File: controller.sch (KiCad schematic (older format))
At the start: 29 parts, among them Q1 Q_PMOS_SGD, Q2 Q_PMOS_SGD, SW1 L1, SW2 L2, SW3 Select, SW4 Start, SW5 R2, SW6 R1, U1 Thumbstick, U2 dpad-cross-trace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

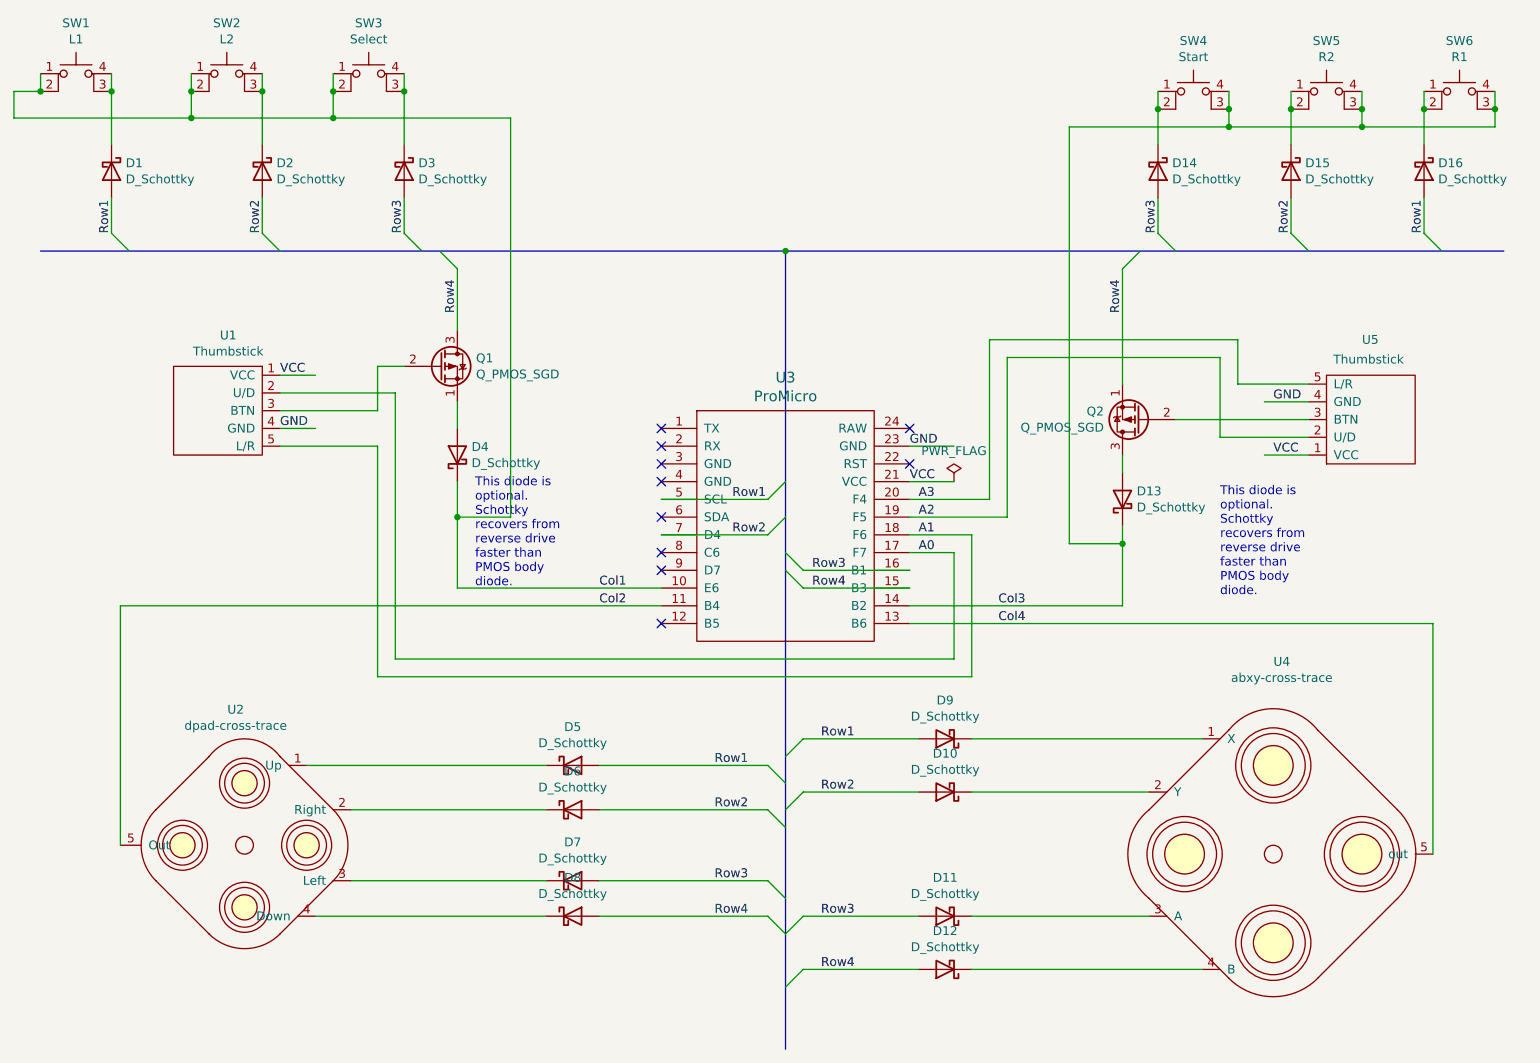
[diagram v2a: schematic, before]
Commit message: Move most PWR_FLAGs into corner and use GNDA.
Use GNDA power pin in the audio subsystem instead of "agnd" sheet label.
Re-examine application of PWR_FLAGS after reading the wiki page.

Change the symbol for thumbstick in controller subsystem to reflect that
it's actually the FPC connector and not actually the thumbstick module.
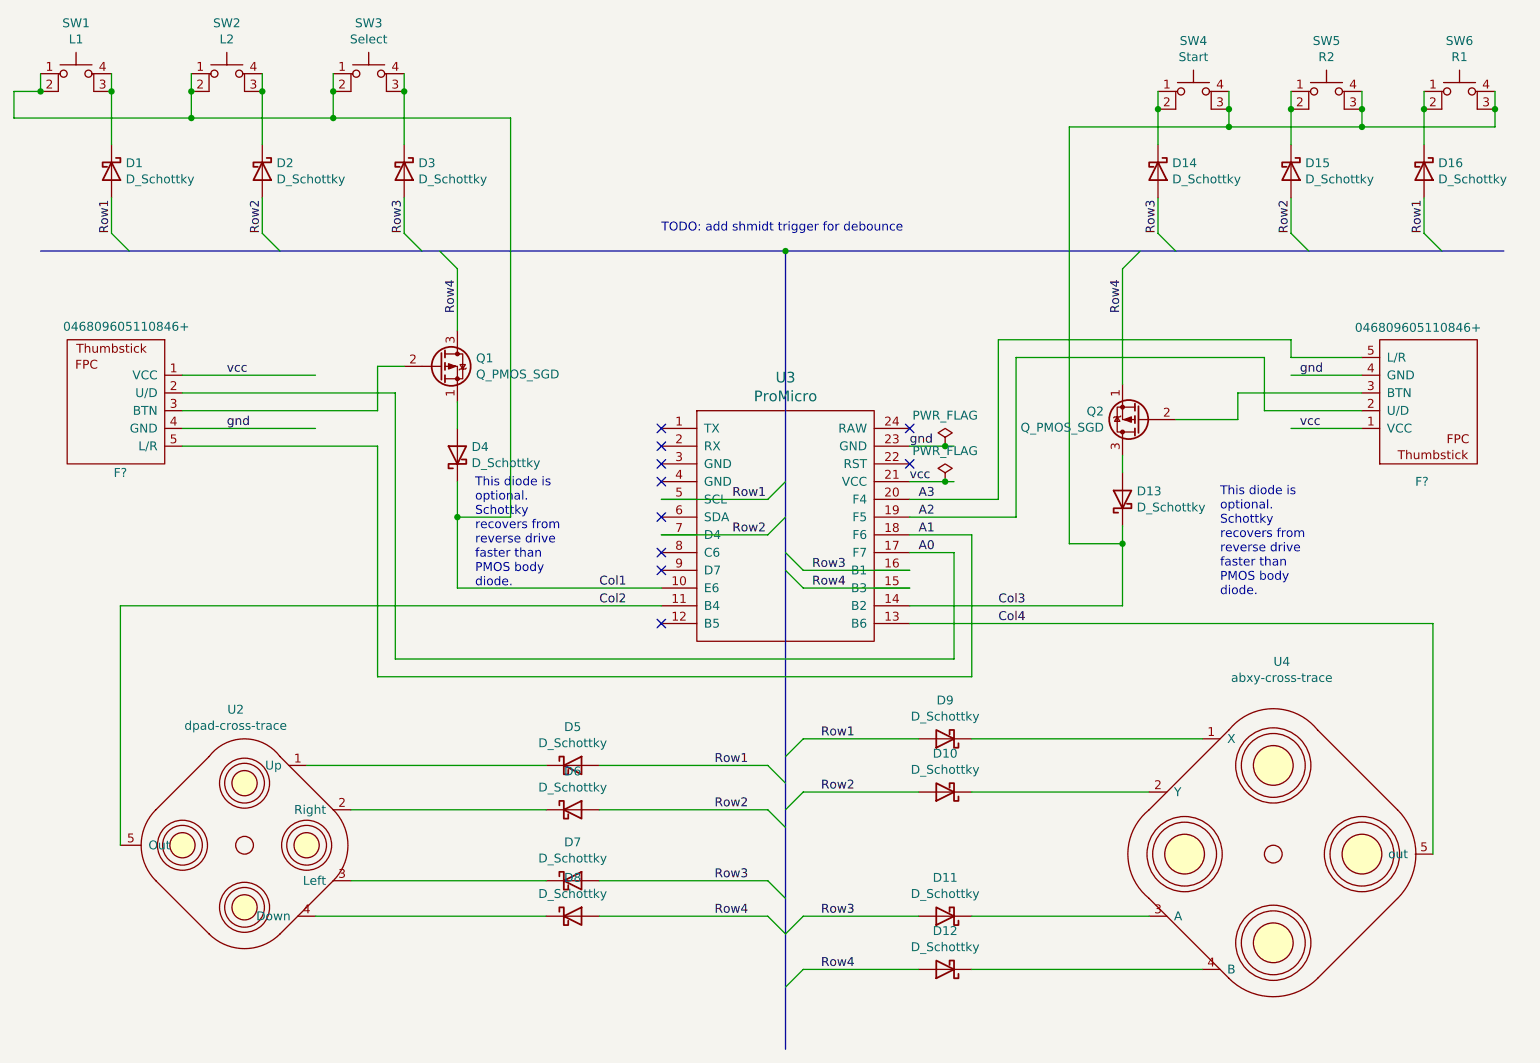
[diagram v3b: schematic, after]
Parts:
- removed U1, U5: Thumbstick, symbol rpi-shell:Thumbstick
- added F? (x2): 046809605110846+, symbol rpi-shell:046809605110846+
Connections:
- net labels added: gnd, vcc
- net labels removed: GND, VCC
- wire segments 105 -> 109
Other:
- note added: "TODO: add shmidt trigger for debounce"
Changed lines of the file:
@@
 $Descr USLetter 11000 8500
 encoding utf-8
-Sheet 2 3
+Sheet 3 3
 Title "RPI Shell Controller Subsystem"
 Date "2021-03-31"
@@
 	-1   0    0    1
 $EndComp
-$Comp
-L rpi-shell:Thumbstick U1
-U 1 1 60680B4A
-P 2650 3000
-F 0 "U1" H 2708 3425 50  0000 C CNN
-F 1 "Thumbstick" H 2708 3334 50  0000 C CNN
-F 2 "" H 2650 3150 50  0001 C CNN
-F 3 "" H 2650 3150 50  0001 C CNN
-	1    2650 3000
-	1    0    0    -1
-$EndComp
-$Comp
-L rpi-shell:Thumbstick U5
-U 1 1 60680B50
-P 9150 3050
-F 0 "U5" H 9200 2600 50  0000 R CNN
-F 1 "Thumbstick" H 9362 2711 50  0000 R CNN
-F 2 "" H 9150 3200 50  0001 C CNN
-F 3 "" H 9150 3200 50  0001 C CNN
-	1    9150 3050
-	-1   0    0    1
-$EndComp
-Wire Wire Line
-	8800 3050 8050 3050
 Wire Wire Line
 	4000 4000 5150 4000
@@
 	7750 4100 6550 4100
 Wire Wire Line
-	3000 3200 3550 3200
+	2450 3200 3550 3200
 Wire Wire Line
 	3550 3200 3550 4500
@@
 	3650 4400 6800 4400
 Wire Wire Line
-	3000 2900 3650 2900
+	2450 2900 3650 2900
 Wire Wire Line
 	3650 2900 3650 4400
 Wire Wire Line
-	3000 2800 3200 2800
-Text Label 3000 2800 0    50   ~ 0
-VCC
-Wire Wire Line
-	6550 3400 6800 3400
-Wire Wire Line
-	8800 3250 8550 3250
-Text Label 8600 3250 0    50   ~ 0
-VCC
+	2450 2800 3200 2800
+Text Label 2700 2800 0    50   ~ 0
+vcc
+Wire Wire Line
+	6550 3400 6750 3400
+Wire Wire Line
+	9100 3100 8700 3100
+Text Label 8750 3100 0    50   ~ 0
+vcc
 Text Label 6550 3400 0    50   ~ 0
-VCC
-Wire Wire Line
-	3000 3100 3200 3100
-Wire Wire Line
-	8800 2950 8550 2950
-Wire Wire Line
-	6550 3200 6800 3200
+vcc
+Wire Wire Line
+	2450 3100 3200 3100
+Wire Wire Line
+	9100 2800 8700 2800
+Wire Wire Line
+	6550 3200 6750 3200
 Text Label 6550 3200 0    50   ~ 0
-GND
-Text Label 8600 2950 0    50   ~ 0
-GND
-Text Label 3000 3100 0    50   ~ 0
-GND
+gnd
+Text Label 8750 2800 0    50   ~ 0
+gnd
+Text Label 2700 3100 0    50   ~ 0
+gnd
 Connection ~ 5850 2100
 Entry Wire Line
@@
 	3550 2750 3550 3000
 Wire Wire Line
-	3550 3000 3000 3000
+	3550 3000 2450 3000
 $Comp
 L Device:D_Schottky D4
@@
 	7750 3750 7750 4100
 Wire Wire Line
-	8400 2850 8400 2600
-Wire Wire Line
-	8400 2600 7000 2600
-Wire Wire Line
-	7000 2600 7000 3500
-Wire Wire Line
-	7000 3500 6550 3500
-Wire Wire Line
-	8400 2850 8800 2850
-Wire Wire Line
-	8300 3150 8300 2700
-Wire Wire Line
-	8300 2700 7100 2700
-Wire Wire Line
-	7100 2700 7100 3600
-Wire Wire Line
-	7100 3600 6550 3600
-Wire Wire Line
-	8300 3150 8800 3150
+	8700 2700 8700 2600
+Wire Wire Line
+	8700 2600 7050 2600
+Wire Wire Line
+	7050 2600 7050 3500
+Wire Wire Line
+	7050 3500 6550 3500
+Wire Wire Line
+	8700 2700 9100 2700
+Wire Wire Line
+	8550 3000 8550 2700
+Wire Wire Line
+	8550 2700 7150 2700
+Wire Wire Line
+	7150 2700 7150 3600
+Wire Wire Line
+	7150 3600 6550 3600
+Wire Wire Line
+	8550 3000 9100 3000
 Text Notes 8300 4050 0    50   ~ 0
 This diode is\noptional.\nSchottky\nrecovers from\nreverse drive\nfaster than \nPMOS body \ndiode.\n
@@
 NoConn ~ 6550 3300
 NoConn ~ 6550 3100
+Text Notes 5150 2000 0    50   ~ 0
+TODO: add shmidt trigger for debounce
+$Comp
+L power:PWR_FLAG #FLG0103
+U 1 1 6070BFBD
+P 6750 3200
+F 0 "#FLG0103" H 6750 3275 50  0001 C CNN
+F 1 "PWR_FLAG" H 6750 3373 50  0000 C CNN
+F 2 "" H 6750 3200 50  0001 C CNN
+F 3 "~" H 6750 3200 50  0001 C CNN
+	1    6750 3200
+	1    0    0    -1
+$EndComp
+Connection ~ 6750 3200
+Wire Wire Line
+	6750 3200 6800 3200
 $Comp
 L power:PWR_FLAG #FLG0104
-U 1 1 606B0D7F
-P 6800 3400
-F 0 "#FLG0104" H 6800 3475 50  0001 C CNN
-F 1 "PWR_FLAG" H 6800 3573 50  0000 C CNN
-F 2 "" H 6800 3400 50  0001 C CNN
-F 3 "~" H 6800 3400 50  0001 C CNN
-	1    6800 3400
-	1    0    0    -1
-$EndComp
+U 1 1 6070C5D5
+P 6750 3400
+F 0 "#FLG0104" H 6750 3475 50  0001 C CNN
+F 1 "PWR_FLAG" H 6750 3573 50  0000 C CNN
+F 2 "" H 6750 3400 50  0001 C CNN
+F 3 "~" H 6750 3400 50  0001 C CNN
+	1    6750 3400
+	1    0    0    -1
+$EndComp
+Connection ~ 6750 3400
+Wire Wire Line
+	6750 3400 6800 3400
+$Comp
+L rpi-shell:046809605110846+ F?
+U 1 1 6079299E
+P 2100 2850
+F 0 "F?" H 2100 2350 50  0000 C CNN
+F 1 "046809605110846+" H 2133 3174 50  0000 C CNN
+F 2 "" H 2100 3000 50  0001 C CNN
+F 3 "" H 2100 3000 50  0001 C CNN
+	1    2100 2850
+	1    0    0    -1
+$EndComp
+$Comp
+L rpi-shell:046809605110846+ F?
+U 1 1 607935EE
+P 9450 3050
+F 0 "F?" H 9500 3400 50  0000 R CNN
+F 1 "046809605110846+" H 9840 2532 50  0000 R CNN
+F 2 "" H 9450 3200 50  0001 C CNN
+F 3 "" H 9450 3200 50  0001 C CNN
+	1    9450 3050
+	-1   0    0    1
+$EndComp
+Wire Wire Line
+	9100 2900 8400 2900
+Wire Wire Line
+	8400 2900 8400 3050
+Wire Wire Line
+	8400 3050 8050 3050
 Wire Bus Line
 	5850 2100 9900 2100

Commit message: Reassign schematic annotation
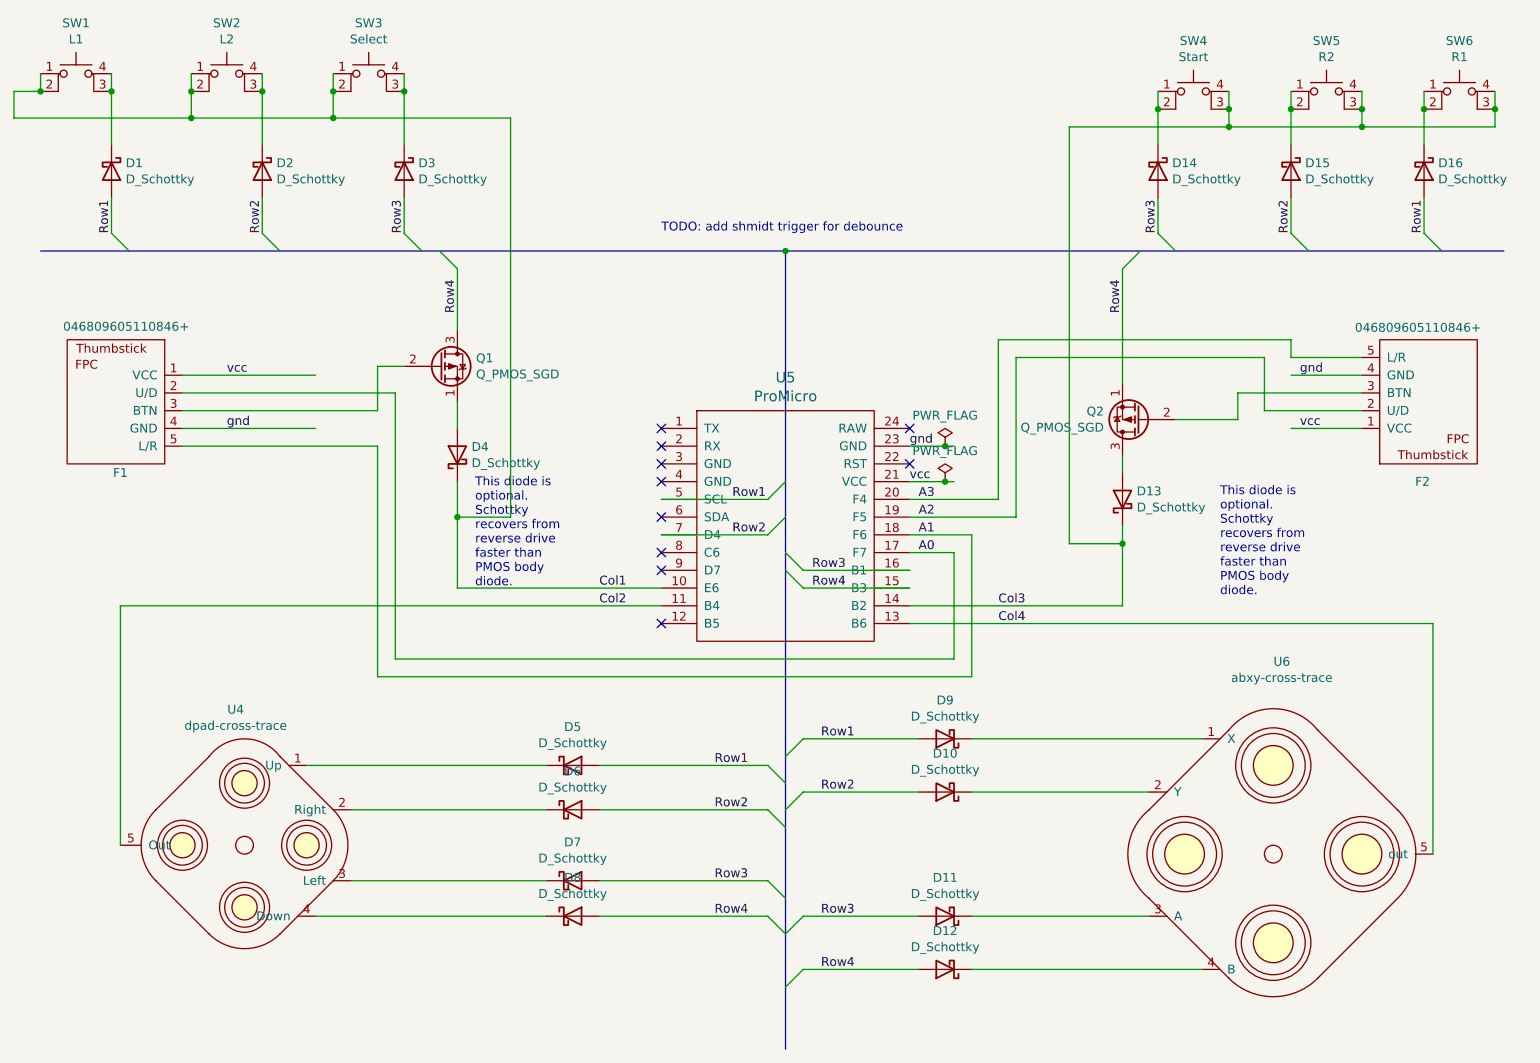
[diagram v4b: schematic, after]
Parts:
- gave numbers to parts that had none: 2
- renumbered U2 to U4, U3 to U5, U4 to U6
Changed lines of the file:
@@
 	4000 4000 5150 4000
 $Comp
-L promicro:ProMicro U3
+L promicro:ProMicro U5
 U 1 1 60680B58
 P 5850 3850
-F 0 "U3" H 5850 4887 60  0000 C CNN
+F 0 "U5" H 5850 4887 60  0000 C CNN
 F 1 "ProMicro" H 5850 4781 60  0000 C CNN
 F 2 "" H 5950 2800 60  0000 C CNN
@@
 Col4
 $Comp
-L rpi-shell:dpad-cross-trace U2
+L rpi-shell:dpad-cross-trace U4
 U 1 1 60680C54
 P 2800 5450
-F 0 "U2" H 2750 6215 50  0000 C CNN
+F 0 "U4" H 2750 6215 50  0000 C CNN
 F 1 "dpad-cross-trace" H 2750 6124 50  0000 C CNN
 F 2 "" H 2800 4400 50  0001 C CNN
@@
 $EndComp
 $Comp
-L rpi-shell:abxy-cross-trace U4
+L rpi-shell:abxy-cross-trace U6
 U 1 1 60680C6A
 P 8600 5500
-F 0 "U4" H 8648 6585 50  0000 C CNN
+F 0 "U6" H 8648 6585 50  0000 C CNN
 F 1 "abxy-cross-trace" H 8648 6494 50  0000 C CNN
 F 2 "" H 8600 5500 50  0001 C CNN
@@
 TODO: add shmidt trigger for debounce
 $Comp
-L power:PWR_FLAG #FLG0103
+L power:PWR_FLAG #FLG04
 U 1 1 6070BFBD
 P 6750 3200
-F 0 "#FLG0103" H 6750 3275 50  0001 C CNN
+F 0 "#FLG04" H 6750 3275 50  0001 C CNN
 F 1 "PWR_FLAG" H 6750 3373 50  0000 C CNN
 F 2 "" H 6750 3200 50  0001 C CNN
@@
 	6750 3200 6800 3200
 $Comp
-L power:PWR_FLAG #FLG0104
+L power:PWR_FLAG #FLG05
 U 1 1 6070C5D5
 P 6750 3400
-F 0 "#FLG0104" H 6750 3475 50  0001 C CNN
+F 0 "#FLG05" H 6750 3475 50  0001 C CNN
 F 1 "PWR_FLAG" H 6750 3573 50  0000 C CNN
 F 2 "" H 6750 3400 50  0001 C CNN
@@
 	6750 3400 6800 3400
 $Comp
-L rpi-shell:046809605110846+ F?
+L rpi-shell:046809605110846+ F1
 U 1 1 6079299E
 P 2100 2850
-F 0 "F?" H 2100 2350 50  0000 C CNN
+F 0 "F1" H 2100 2350 50  0000 C CNN
 F 1 "046809605110846+" H 2133 3174 50  0000 C CNN
 F 2 "" H 2100 3000 50  0001 C CNN
@@
 $EndComp
 $Comp
-L rpi-shell:046809605110846+ F?
+L rpi-shell:046809605110846+ F2
 U 1 1 607935EE
 P 9450 3050
-F 0 "F?" H 9500 3400 50  0000 R CNN
+F 0 "F2" H 9500 3400 50  0000 R CNN
 F 1 "046809605110846+" H 9840 2532 50  0000 R CNN
 F 2 "" H 9450 3200 50  0001 C CNN
